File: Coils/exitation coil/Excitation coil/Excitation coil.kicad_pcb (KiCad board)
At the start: 2 copper layers, 74.8 x 56.5 mm, 7 parts, among them J1 Conn_01x02_Socket, J2 Conn_01x02_Pin

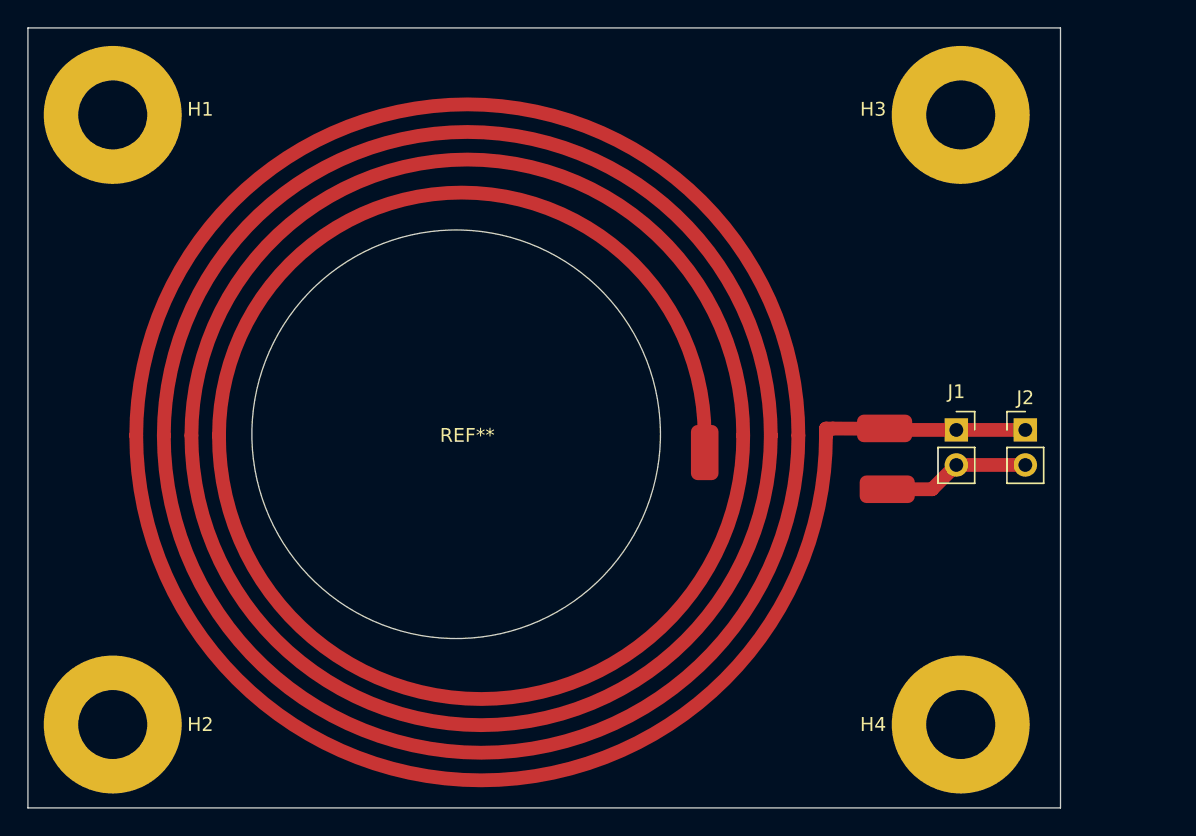
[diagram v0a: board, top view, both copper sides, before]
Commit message: added 3d models for OPA3692, THS3091 and BNC connector
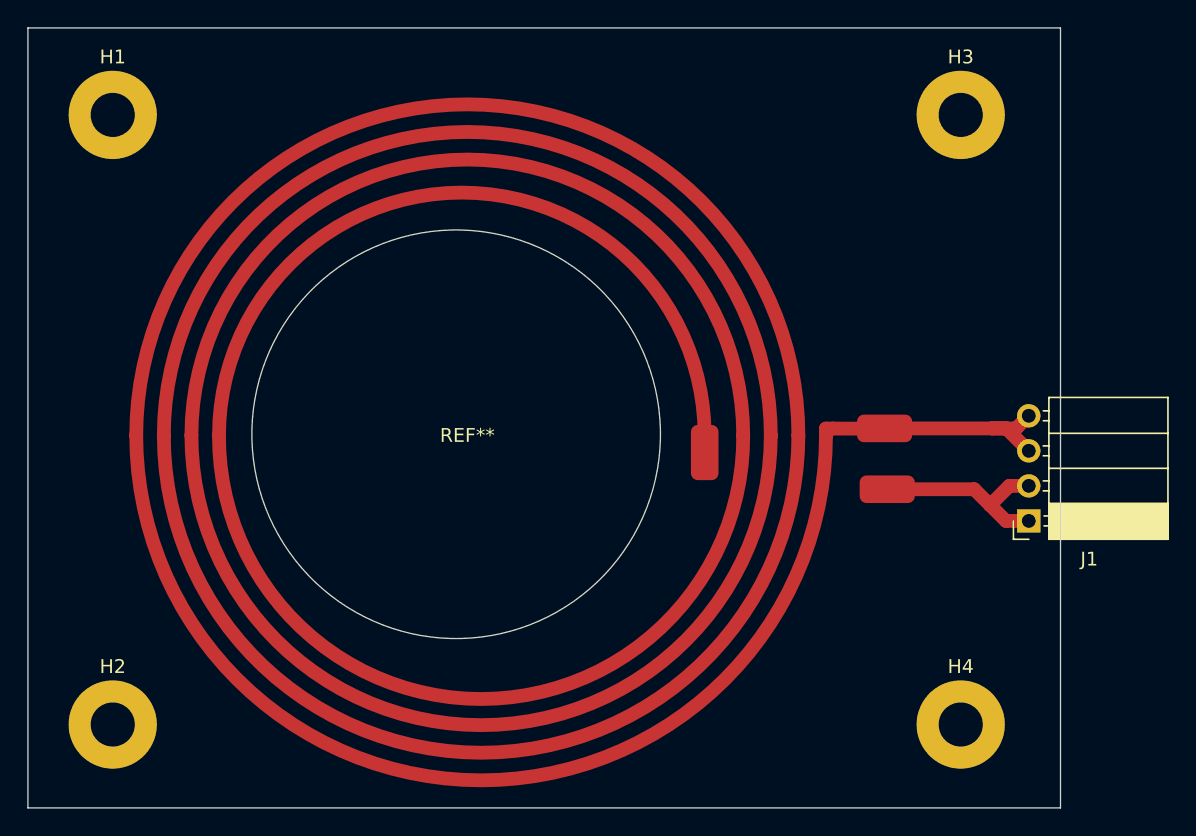
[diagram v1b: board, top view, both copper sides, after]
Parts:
- removed J2: Conn_01x02_Pin, Connector_PinHeader_2.54mm:PinHeader_1x02_P2.54mm_Vertical
- H1, H2, H3, H4: footprint MountingHole:MountingHole_5mm_Pad -> MountingHole:MountingHole_3.2mm_M3_Pad
- J1: value Conn_01x02_Socket -> Conn_01x04_Socket; footprint Connector_PinSocket_2.54mm:PinSocket_1x02_P2.54mm_Vertical -> Connector_PinSocket_2.54mm:PinSocket_1x04_P2.54mm_Horizontal
- moved J1 8.43 mm to (181.7, 103.2), turned to 180 degrees
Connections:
- J1 pad 1: /coil start -> /coil end
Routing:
- net /coil start: track 10.8 -> 14.2 mm
- net /coil end: track 11.5 -> 14.6 mm

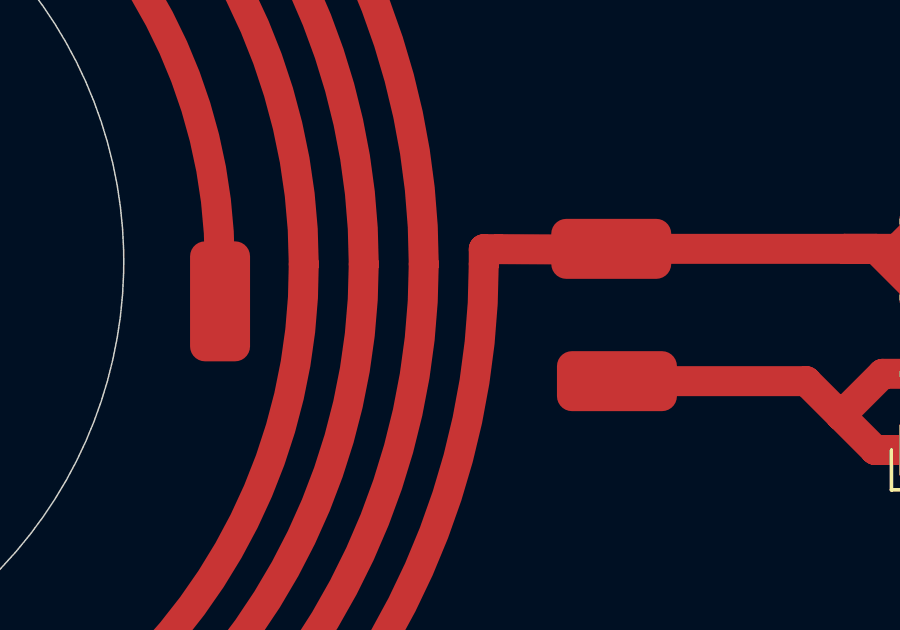
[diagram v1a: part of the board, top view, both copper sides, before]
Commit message: Small corrections, changed footprint for edge SMA connectors
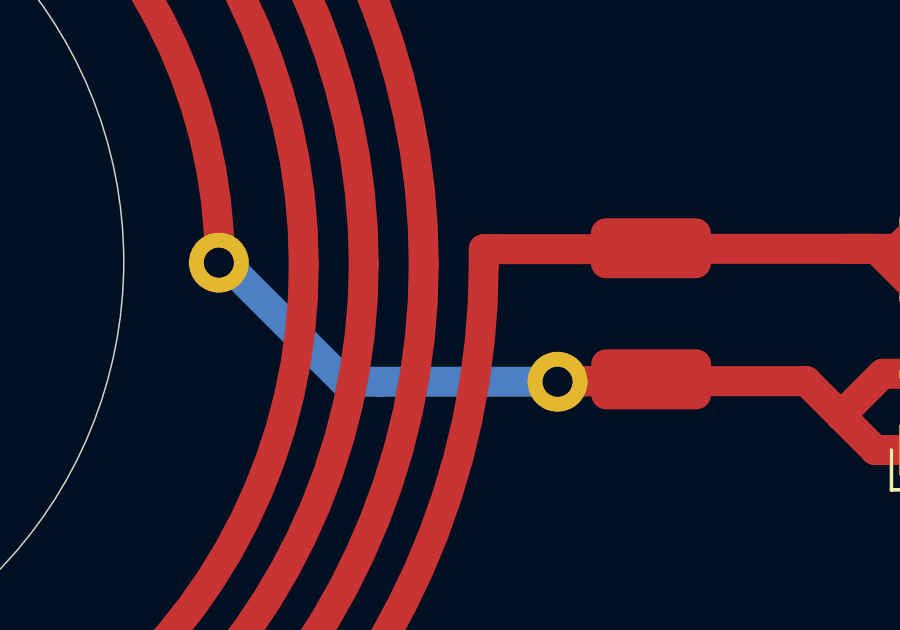
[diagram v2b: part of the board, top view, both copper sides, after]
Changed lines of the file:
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@@
 		)
 		(fp_line
-			(start 26.5 -0.5)
-			(end 28.88 -0.49)
+			(start 26.4 -0.5)
+			(end 31.565 -0.5)
+			(stroke
+				(width 1)
+				(type default)
+			)
+			(layer "F.Cu")
+		)
+		(fp_line
+			(start 28.44 3.9)
+			(end 30.44 3.9)
+			(stroke
+				(width 1)
+				(type default)
+			)
+			(layer "F.Cu")
+		)
+		(fp_line
+			(start 28.46 3.9)
+			(end 30.44 3.9)
+			(stroke
+				(width 1)
+				(type default)
+			)
+			(layer "F.Cu")
+		)
+		(fp_line
+			(start 30.44 3.9)
+			(end 28.46 3.9)
+			(stroke
+				(width 1)
+				(type default)
+			)
+			(layer "F.Cu")
+		)
+		(fp_line
+			(start 30.44 3.9)
+			(end 28.46 3.9)
 			(stroke
 				(width 1)
@@
 			(layer "F.Cu")
 		)
+		(fp_line
+			(start 21.35 3.92)
+			(end 17.17 -0.26)
+			(stroke
+				(width 1)
+				(type default)
+			)
+			(layer "B.Cu")
+		)
+		(fp_line
+			(start 22.51 3.92)
+			(end 21.35 3.92)
+			(stroke
+				(width 1)
+				(type default)
+			)
+			(layer "B.Cu")
+		)
+		(fp_line
+			(start 28.46 3.92)
+			(end 22.51 3.92)
+			(stroke
+				(width 1)
+				(type default)
+			)
+			(layer "B.Cu")
+		)
 		(fp_text user "${REFERENCE}"
 			(at 0 0 0)
@@
 			)
 		)
-		(pad "" smd roundrect
-			(at 17.21 1.24 90)
-			(size 4 2)
-			(layers "F.Cu")
-			(roundrect_rratio 0.25)
+		(pad "" thru_hole circle
+			(at 17.17 -0.05 90)
+			(size 2 2)
+			(drill 1)
+			(layers "*.Cu" "*.Mask")
+			(remove_unused_layers no)
+		)
+		(pad "" thru_hole circle
+			(at 28.46 3.92 90)
+			(size 2 2)
+			(drill 1)
+			(layers "*.Cu" "*.Mask")
+			(remove_unused_layers no)
 		)
 		(pad "1" smd roundrect
-			(at 30.25 -0.51)
+			(at 31.57 -0.53)
 			(size 4 2)
 			(layers "F.Cu")
@@
 		)
 		(pad "2" smd roundrect
-			(at 30.44 3.9)
+			(at 31.58 3.84)
 			(size 4 2)
 			(layers "F.Cu")
@@
 		)
 		(fp_text user "${REFERENCE}"
-			(at -5.775 3.81 270)
-			(layer "F.Fab")
-			(effects
+			(at -5.775 3.81 -90)
+			(layer "F.Fab")
+			(effects

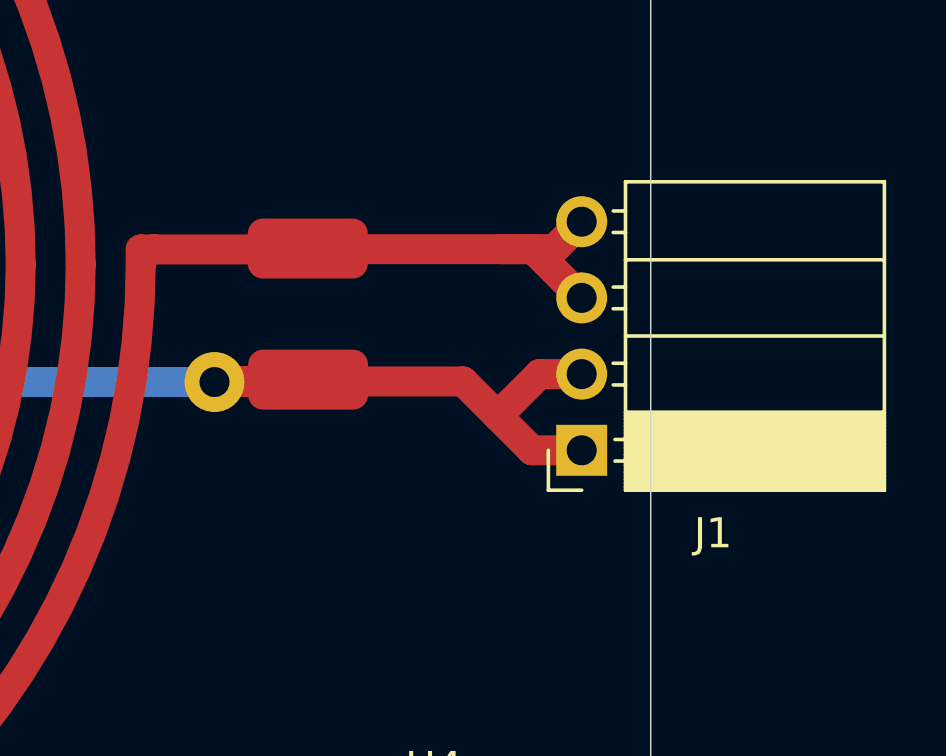
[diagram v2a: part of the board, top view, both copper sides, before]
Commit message: Added via stiching to TX board, moved almost all vias off of pads, increased the trace width for the power supply and changed coil connector to horizontal socket
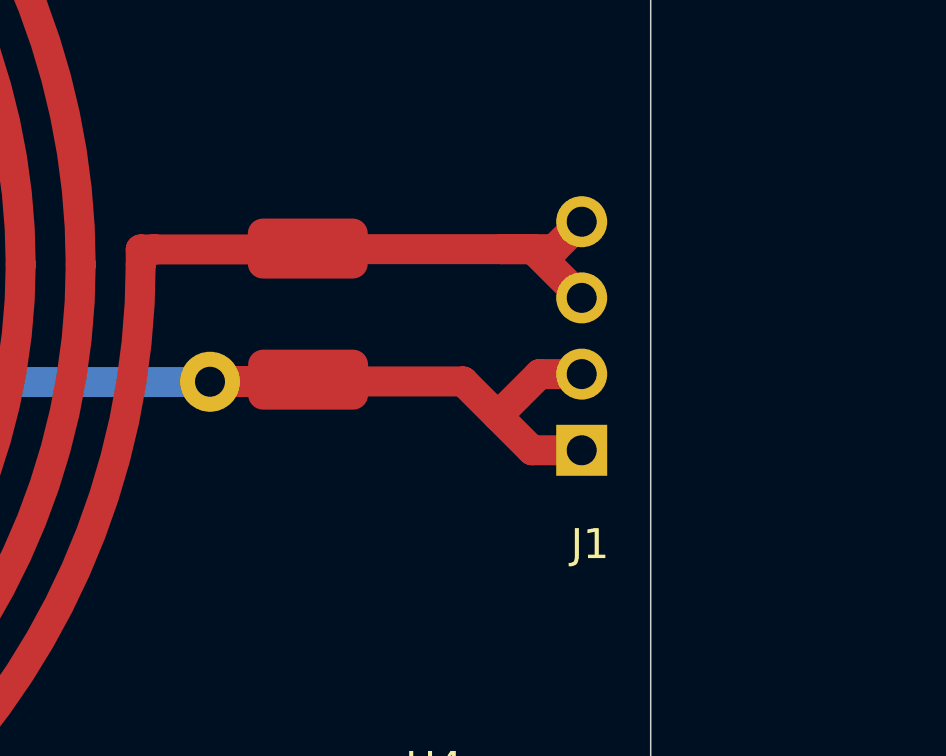
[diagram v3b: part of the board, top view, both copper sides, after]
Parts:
- J1: value Conn_01x04_Socket -> Conn_01x04; footprint Connector_PinSocket_2.54mm:PinSocket_1x04_P2.54mm_Horizontal -> Connector_PinHeader_2.54mm:PinHeader_1x04_P2.54mm_Horizontal; moved to B.Cu
- turned J1 to 0 degrees

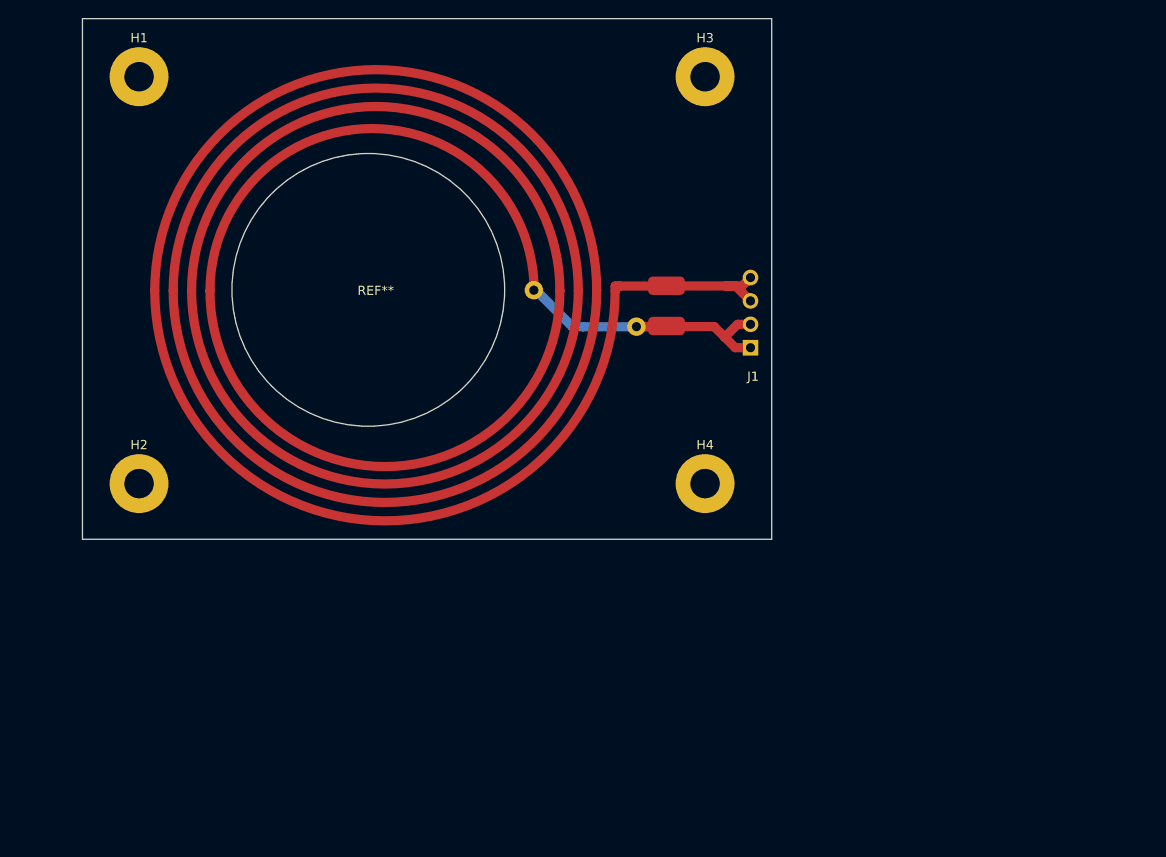
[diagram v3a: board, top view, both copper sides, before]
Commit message: Drew a footprint for a BNC edge connector 112640, made sure coils are centered and as symmetrical as possible:wq
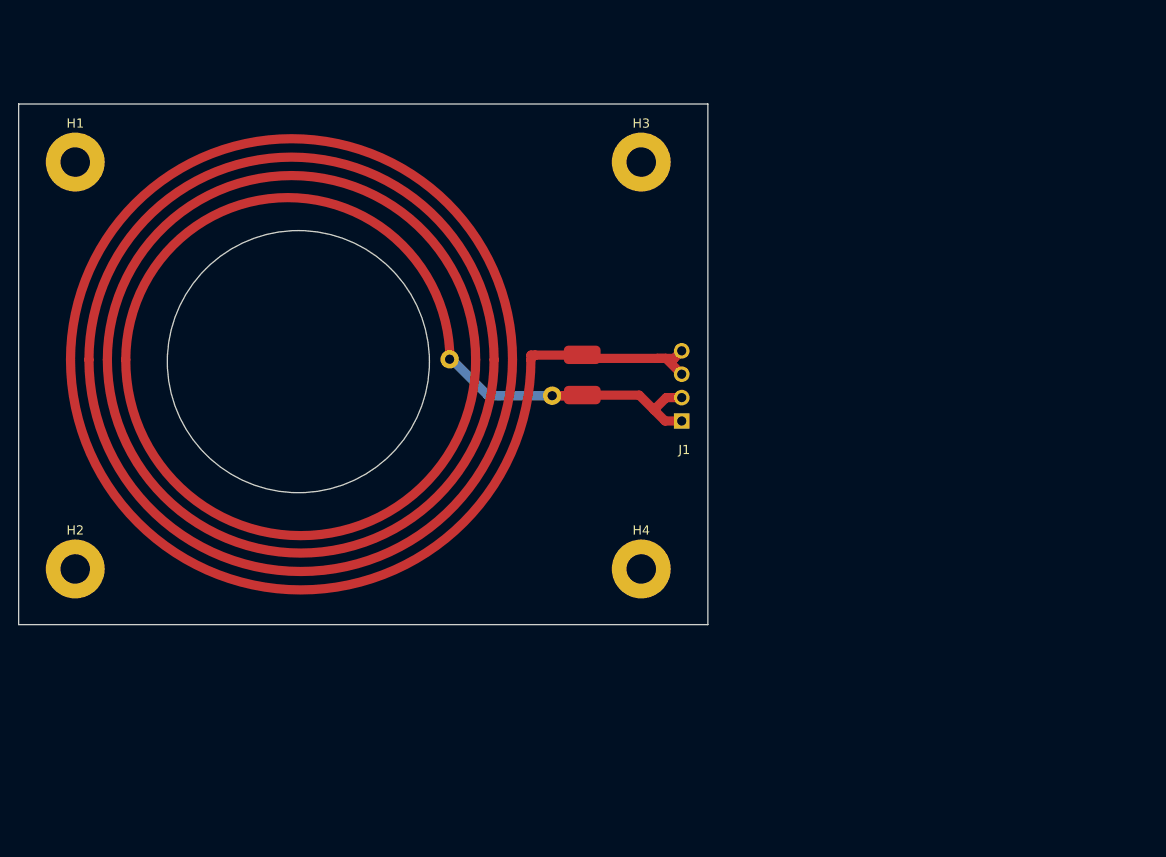
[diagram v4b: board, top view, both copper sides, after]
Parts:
- moved REF** 11.8 mm to (131.9, 104.5)
- moved H1 11.6 mm to (108.4, 83.0)
- moved H2 11.6 mm to (108.4, 127.2)
- moved H3 11.6 mm to (169.8, 83.0)
- moved H4 11.6 mm to (169.8, 127.2)
- moved J1 10.9 mm to (174.2, 111.2)
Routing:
- net /coil end: track 14.6 -> 15.5 mm
- net /coil start: track 14.2 -> 14.7 mm
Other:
- outline, holes or cut-outs redrawn
